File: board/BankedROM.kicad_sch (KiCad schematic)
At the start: 16 parts, among them U28 AT29C040, U29 AT29C040, U30 AT29C040, U31 AT29C040, U32 AT29C040, U33 AT29C040, U34 AT29C040, U35 AT29C040

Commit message: V1.2B: Final for production.
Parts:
- U28, U29, U30, U31, U32, U33, U34, U35: value AT29C040 -> SST39SF040; symbol Memory_EPROM:27C040 -> Memory_Flash:SST39SF040
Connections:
- net RWB is gone; now on net ROMB4: U28.1 (A18), U29.1 (A18), U30.1 (A18), U31.1 (A18), U32.1 (A18), U33.1 (A18), U34.1 (A18), U35.1 (A18)
- net +5V: now also C35.2, C36.2, C37.2, C39.2, C40.2, C41.2, C42.2, U28.31 (PGM), U29.31 (PGM), U30.31 (PGM), U31.31 (PGM), U32.31 (PGM), U33.31 (PGM), U34.31 (PGM), U35.31 (PGM); no longer C35.1, C36.1, C37.1, C39.1, C40.1, C41.1, C42.1
- net GND: now also C35.1, C36.1, C37.1, C39.1, C40.1, C41.1, C42.1; no longer C35.2, C36.2, C37.2, C39.2, C40.2, C41.2, C42.2
- net ROMB4: no longer U28.31 (A18), U29.31 (A18), U30.31 (A18), U31.31 (A18), U32.31 (A18), U33.31 (A18), U34.31 (A18), U35.31 (A18)
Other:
- moved on the sheet: C35, C36, C37, C38, C39, C40, C41, C42

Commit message: V1.4E
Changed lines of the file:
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@@
 		)
 	)
+	(wire
+		(pts
+			(xy 147.32 118.11) (xy 147.32 119.38)
+		)
+		(stroke
+			(width 0)
+			(type default)
+		)
+	)
 	(bus
 		(pts
@@
 	(symbol
 		(lib_id "power:+5V")
-		(at 147.32 119.38 0)
+		(at 147.32 118.11 0)
 		(unit 1)
 		(exclude_from_sim no)
@@
 		(dnp no)
 		(property "Reference" "#PWR042"
-			(at 147.32 123.19 0)
+			(at 147.32 121.92 0)
 			(effects
 				(font
@@
 		)
 		(property "Value" "+5V"
-			(at 150.114 117.602 0)
+			(at 150.114 116.332 0)
 			(effects
 				(font
@@
 		)
 		(property "Footprint" ""
-			(at 147.32 119.38 0)
+			(at 147.32 118.11 0)
 			(effects
 				(font
@@
 		)
 		(property "Datasheet" ""
-			(at 147.32 119.38 0)
+			(at 147.32 118.11 0)
 			(effects
 				(font
@@
 		)
 		(property "Description" "Power symbol creates a global label with name \"+5V\""
-			(at 147.32 119.38 0)
+			(at 147.32 118.11 0)
 			(effects
 				(font
@@
 		(dnp no)
 		(property "Reference" "U28"
-			(at 45.72 27.94 0)
+			(at 46.482 26.67 0)
 			(effects
 				(font
@@
 		)
 		(property "Value" "SST39SF040"
-			(at 45.72 30.48 0)
+			(at 46.482 29.21 0)
 			(effects
 				(font

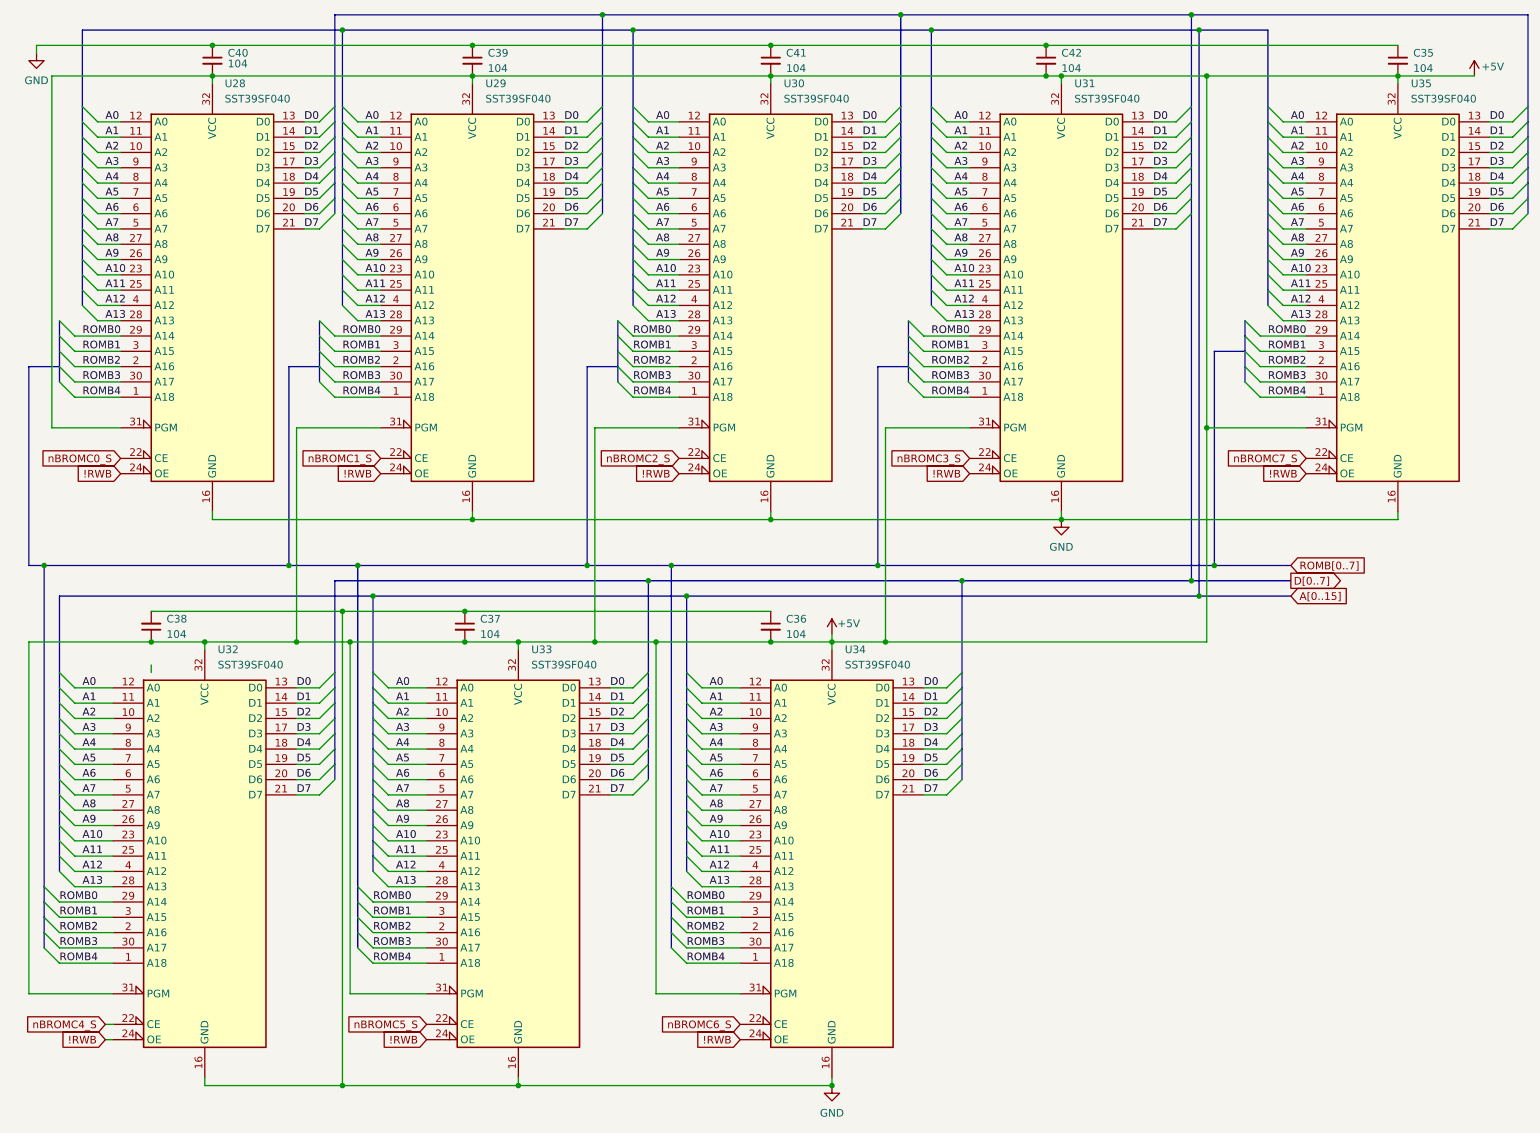
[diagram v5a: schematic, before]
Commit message: Version 1.7A: More rearrangement, partial wiring of PDB, addition of W register
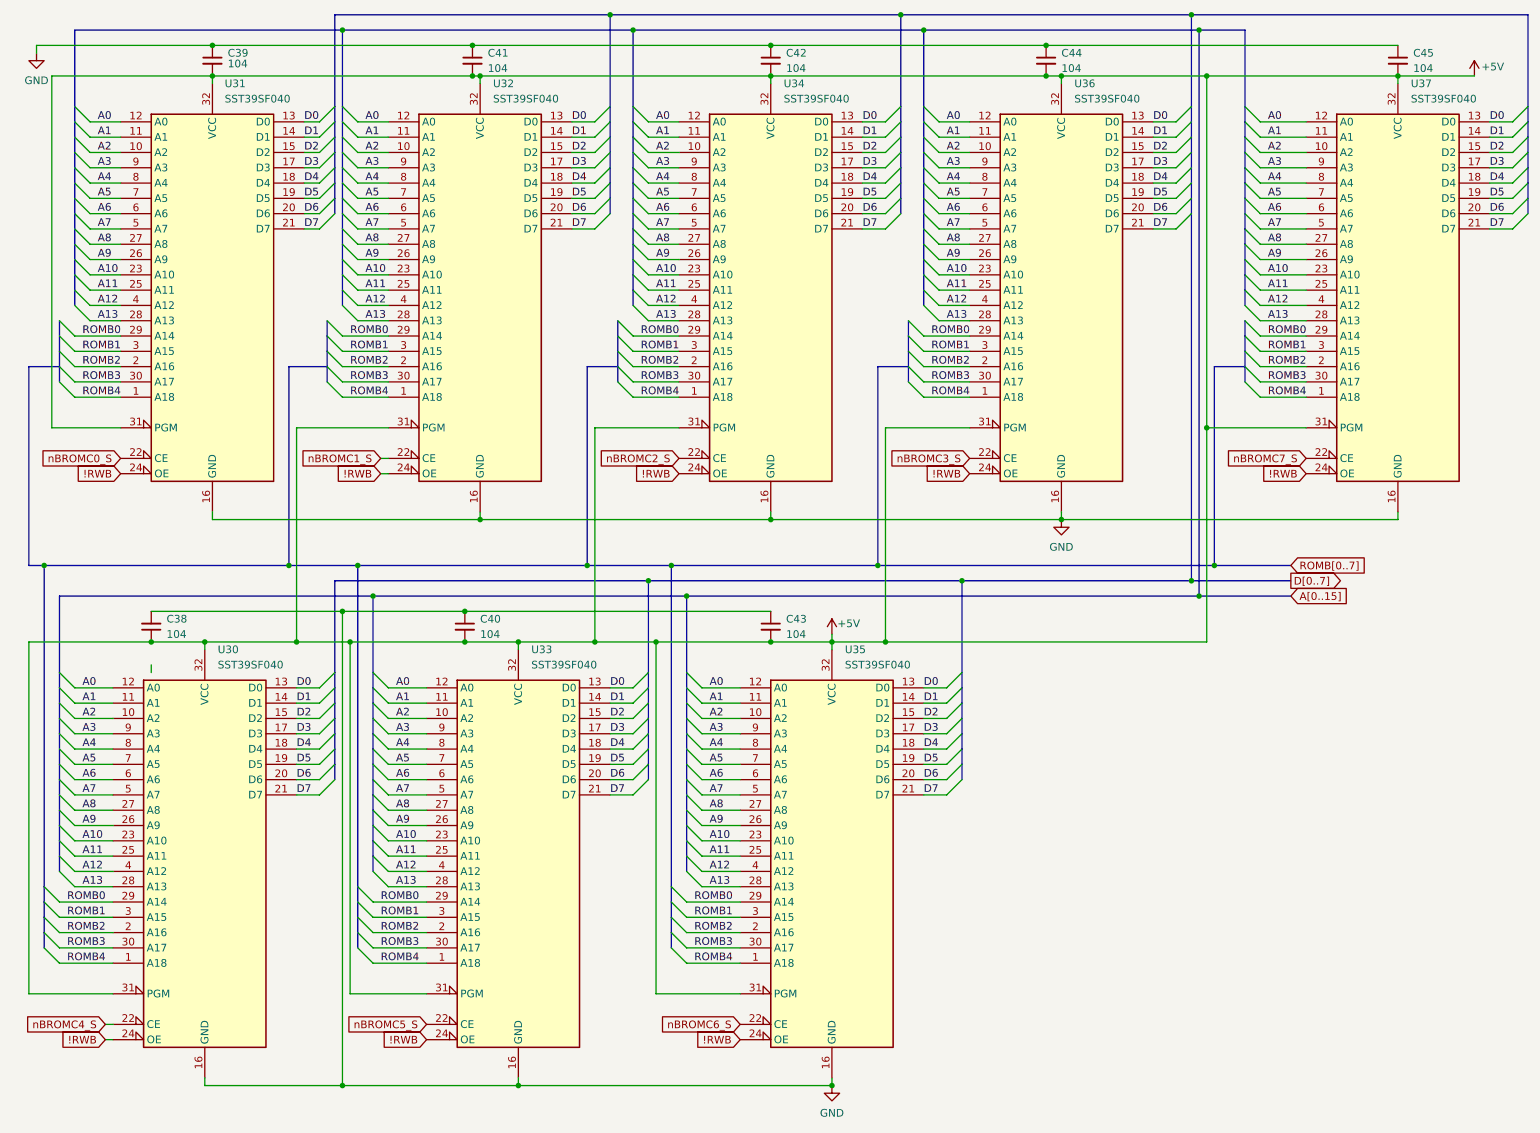
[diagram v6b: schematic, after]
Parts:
- renumbered C40 to C39, C37 to C40, C39 to C41, C41 to C42, C36 to C43, C42 to C44, C35 to C45, U32 to U30, U28 to U31, U29 to U32, U30 to U34, U34 to U35, U31 to U36, U35 to U37
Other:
- moved on the sheet: U32
